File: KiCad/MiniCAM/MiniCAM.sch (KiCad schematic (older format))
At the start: 64 parts, among them J1 SMA-J-P-H-RA-TH1, J2 Conn_01x02, J3 Conn_01x03, U1 NCV8154MW180280TBG, U2 DS90UB933-Q1, U3 MT9P031, U4 SiT_2.5mmx2mm

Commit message: Finish initial schematic, layout, and routing.
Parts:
- removed C17: C_Small, .Capacitor:C_0402_1005Metric_L, symbol .Device:C_Small
- added C? (x2): 10uF, .Capacitor:C_0603_1608Metric_L, symbol .Device:C_Small
- added J4: Conn_02x03_Odd_Even, Connector_PinSocket_1.27mm:PinSocket_2x03_P1.27mm_Horizontal, symbol Connector_Generic:Conn_02x03_Odd_Even
- C11, C16: value C_Small -> 1uF
- C12: value 1uF -> 10uF; footprint .Capacitor:C_0402_1005Metric_L -> .Capacitor:C_0603_1608Metric_L
- C18, C21, C26, C29, C31: value C_Small -> 10nF
- C19, C22, C27, C30, C32: value C_Small -> 0.1uF
- C20, C23, C28: value C_Small -> 4.7uF
- C35: value ?? -> 1uF
- R7, R8: value ?? -> 10K
- R9: value ?? -> 100K
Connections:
- net labels added: DIN0, DIN1, DIN2, DIN3, DIN4, DIN5, DIN6, DIN7, DIN8, DIN9
- net labels removed: SCK
- wire segments 207 -> 221
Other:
- moved on the sheet: J3

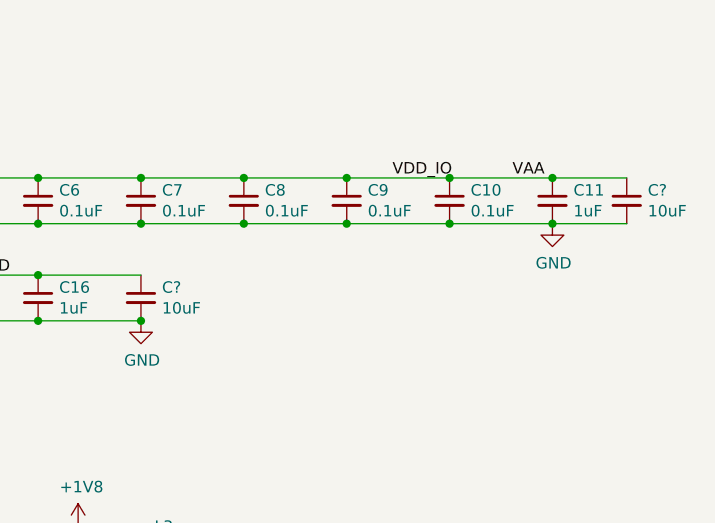
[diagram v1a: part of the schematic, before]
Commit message: Switch 2 and 3 headers from pins to sockets. Generate STEP file.
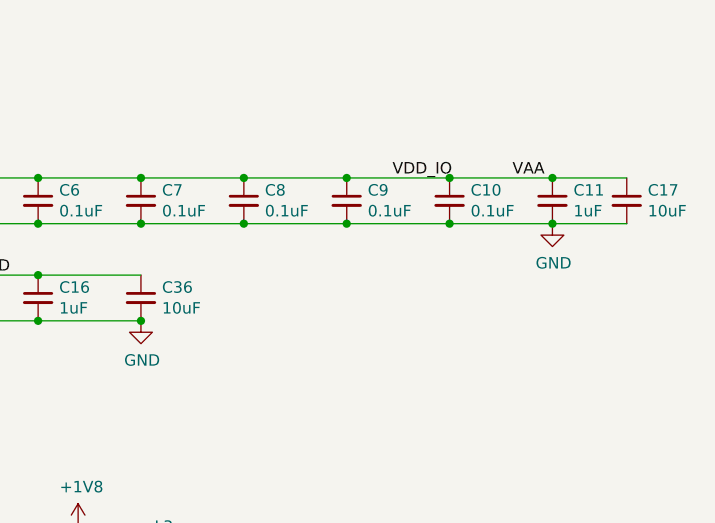
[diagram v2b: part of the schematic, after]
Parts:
- J2: footprint Connector_PinHeader_1.27mm:PinHeader_1x02_P1.27mm_Vertical -> Connector_PinSocket_1.27mm:PinSocket_1x02_P1.27mm_Vertical
- J3: footprint Connector_PinHeader_1.27mm:PinHeader_1x03_P1.27mm_Vertical -> Connector_PinSocket_1.27mm:PinSocket_1x03_P1.27mm_Vertical
- gave numbers to parts that had none: 2
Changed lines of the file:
@@
 F 0 "J2" H 5830 1417 50  0000 L CNN
 F 1 "Conn_01x02" H 5830 1326 50  0000 L CNN
-F 2 "Connector_PinHeader_1.27mm:PinHeader_1x02_P1.27mm_Vertical" H 5750 1425 50  0001 C CNN
+F 2 "Connector_PinSocket_1.27mm:PinSocket_1x02_P1.27mm_Vertical" H 5750 1425 50  0001 C CNN
 F 3 "~" H 5750 1425 50  0001 C CNN
 	1    5750 1425
@@
 F 0 "J3" H 5830 1842 50  0000 L CNN
 F 1 "Conn_01x03" H 5830 1751 50  0000 L CNN
-F 2 "Connector_PinHeader_1.27mm:PinHeader_1x03_P1.27mm_Vertical" H 5750 1800 50  0001 C CNN
+F 2 "Connector_PinSocket_1.27mm:PinSocket_1x03_P1.27mm_Vertical" H 5750 1800 50  0001 C CNN
 F 3 "~" H 5750 1800 50  0001 C CNN
 	1    5750 1800
@@
 Connection ~ 2575 1325
 $Comp
-L .Device:C_Small C?
+L .Device:C_Small C36
 U 1 1 5F776ABC
 P 8975 1350
-F 0 "C?" H 9067 1396 50  0000 L CNN
+F 0 "C36" H 9067 1396 50  0000 L CNN
 F 1 "10uF" H 9067 1305 50  0000 L CNN
 F 2 ".Capacitor:C_0603_1608Metric_L" H 8975 1350 50  0001 C CNN
@@
 Connection ~ 8975 1450
 $Comp
-L .Device:C_Small C?
+L .Device:C_Small C17
 U 1 1 5F779E53
 P 11100 925
-F 0 "C?" H 11192 971 50  0000 L CNN
+F 0 "C17" H 11192 971 50  0000 L CNN
 F 1 "10uF" H 11192 880 50  0000 L CNN
 F 2 ".Capacitor:C_0603_1608Metric_L" H 11100 925 50  0001 C CNN

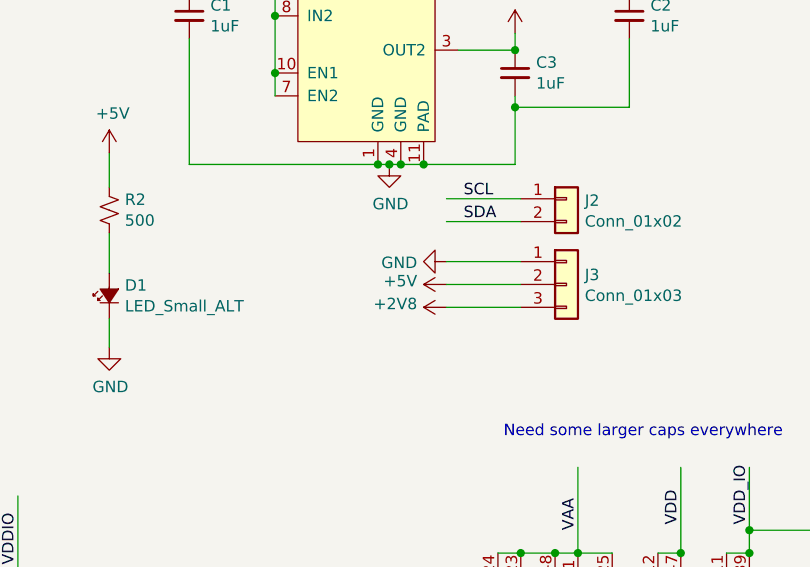
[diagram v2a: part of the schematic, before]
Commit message: Move LED ring headers to a consistent 4mm x 1mm spacing from center on lens.
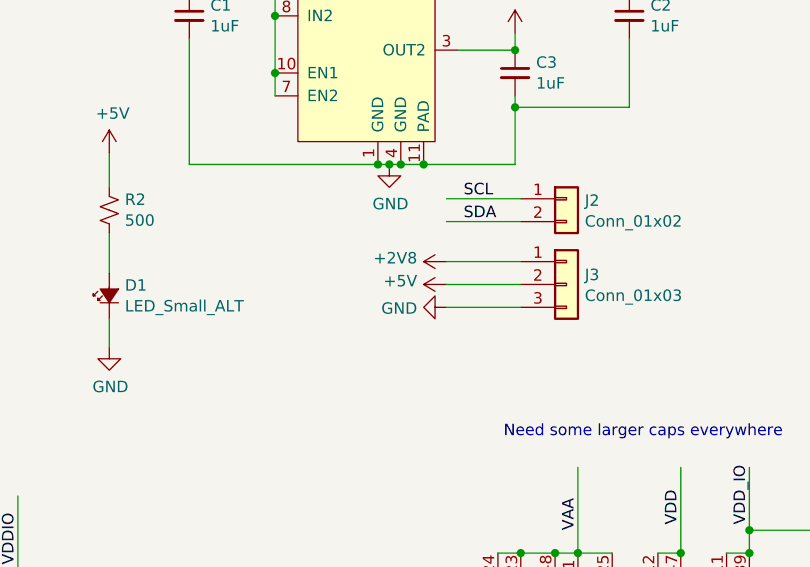
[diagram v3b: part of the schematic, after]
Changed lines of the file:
@@
 L power:GND #PWR0138
 U 1 1 5F6758D2
-P 5225 1700
-F 0 "#PWR0138" H 5225 1450 50  0001 C CNN
-F 1 "GND" V 5230 1572 50  0000 R CNN
-F 2 "" H 5225 1700 50  0001 C CNN
-F 3 "" H 5225 1700 50  0001 C CNN
-	1    5225 1700
+P 5225 1900
+F 0 "#PWR0138" H 5225 1650 50  0001 C CNN
+F 1 "GND" V 5230 1772 50  0000 R CNN
+F 2 "" H 5225 1900 50  0001 C CNN
+F 3 "" H 5225 1900 50  0001 C CNN
+	1    5225 1900
 	0    1    1    0
 $EndComp
@@
 L power:+2V8 #PWR0140
 U 1 1 5F67654A
-P 5225 1900
-F 0 "#PWR0140" H 5225 1750 50  0001 C CNN
-F 1 "+2V8" V 5240 2028 50  0000 L CNN
-F 2 "" H 5225 1900 50  0001 C CNN
-F 3 "" H 5225 1900 50  0001 C CNN
-	1    5225 1900
+P 5225 1700
+F 0 "#PWR0140" H 5225 1550 50  0001 C CNN
+F 1 "+2V8" V 5240 1828 50  0000 L CNN
+F 2 "" H 5225 1700 50  0001 C CNN
+F 3 "" H 5225 1700 50  0001 C CNN
+	1    5225 1700
 	0    -1   -1   0
 $EndComp

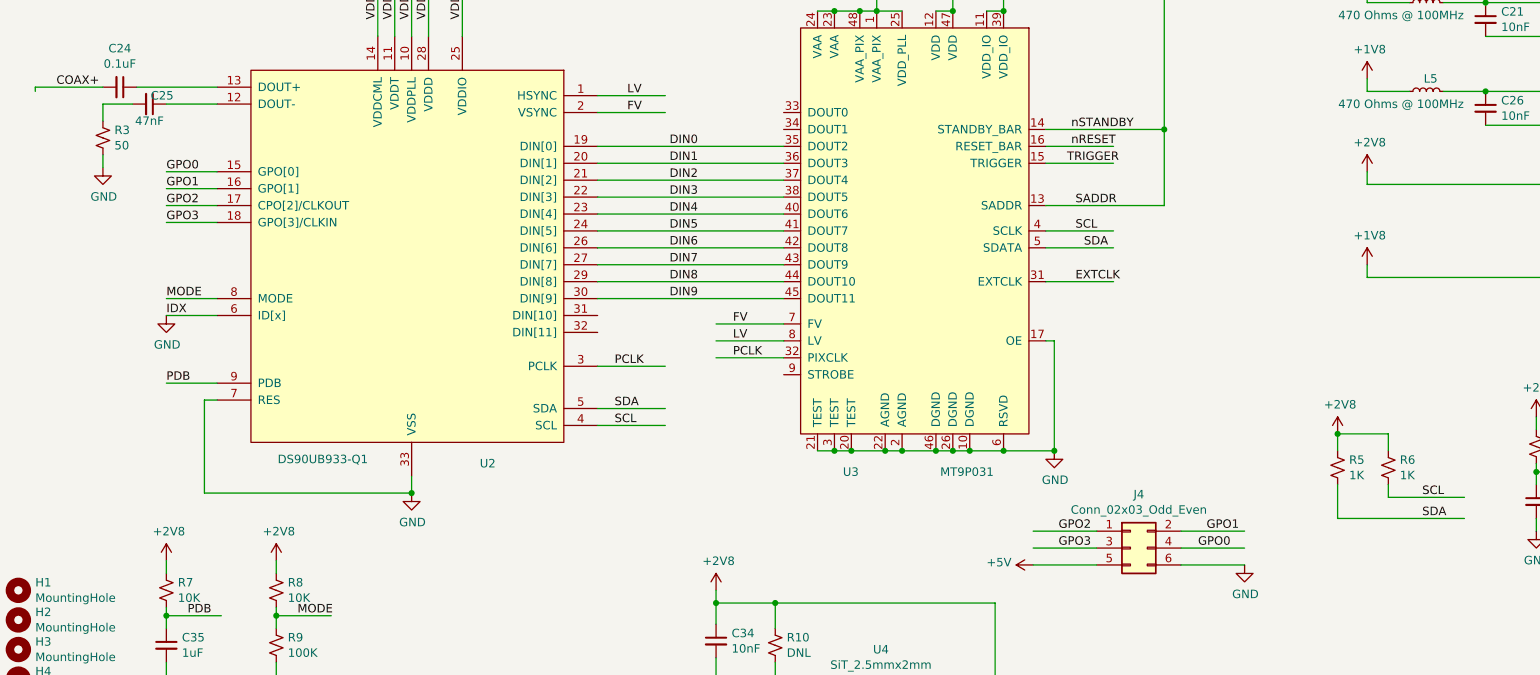
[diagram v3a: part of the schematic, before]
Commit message: Updated LED ring PCB Board
Changed 10UF 0603 to 1210 50V: C1210C106K5RACTU
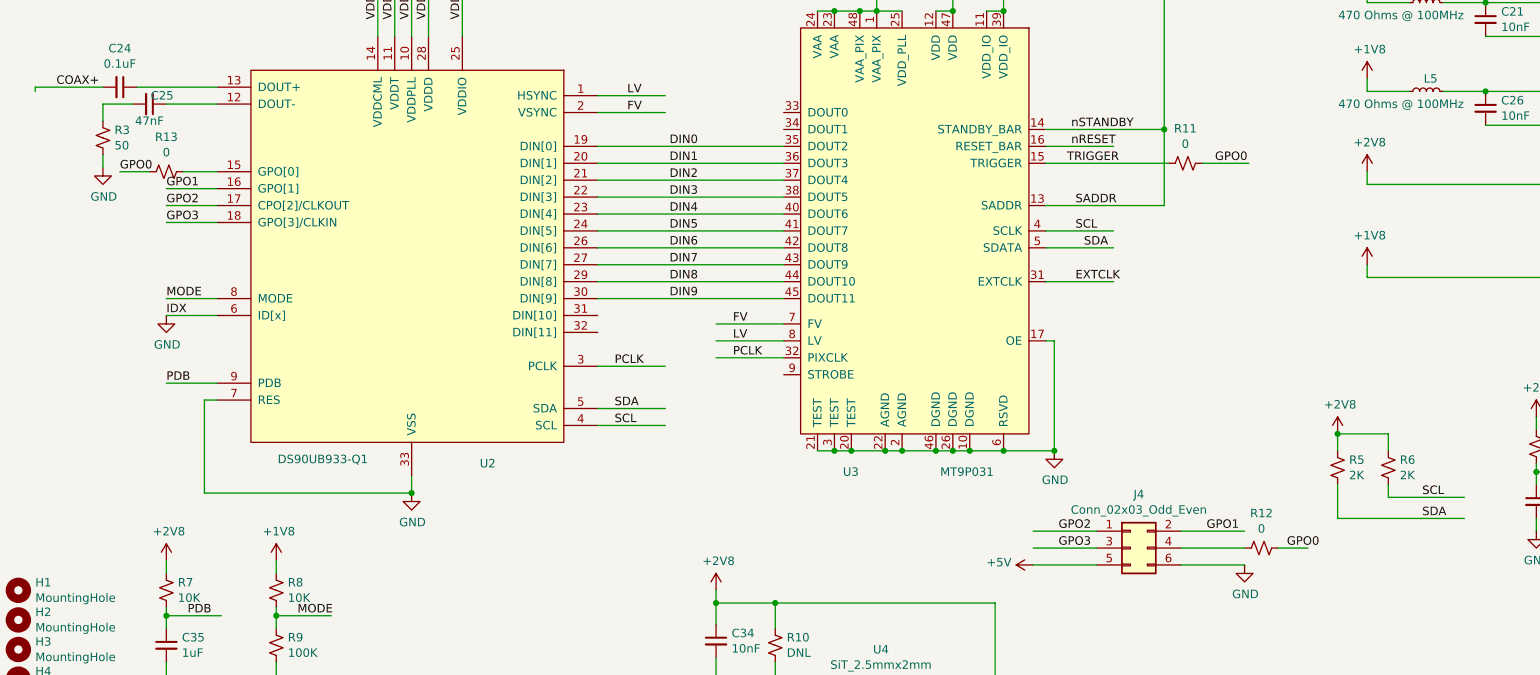
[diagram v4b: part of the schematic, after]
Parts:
- added R11, R12, R13: 0, .Resistor:R_0402_1005Metric_ERJ_L, symbol .Device:R_Small_US
- C1, C11, C16, C2, C3, C33, C35: Part Number (none) -> GRT155R61C105KE01D
- C10, C14, C15, C19, C22, C24, C27, C30, C32, C4, C5, C6, C7, C8, C9: Part Number (none) -> GCM155R71C104KA55J
- C12, C13, C17, C36: Part Number (none) -> GRM188R61A106KE69J
- C18, C21, C26, C29, C31, C34: Part Number (none) -> GCM155R71E103KA37D
- C20, C23, C28: Part Number (none) -> CC0402MRX5R6BB475
- C25: Part Number (none) -> GRM155R71A473KA01D
- D1: Part Number (none) -> LTST-C190KRKT
- H1, H2, H3, H4, H5, H6, J2, J3, J4, R10, U3, U4: Part Number (none) -> DNL
- J1: Part Number (none) -> CONSMA001-SMD-G-T
- L1, L3, L4, L5: Part Number (none) -> BLM18PG471SN1D
- L2: Part Number (none) -> ADL3225V-470MT-TL000
- R1: Part Number (none) -> ERJ-2RKF2001X
- R2: Part Number (none) -> ERJ-2RKF4990X
- R3: Part Number (none) -> ERJ-2RKF49R9X
- R4: Part Number (none) -> ERJ-2GEJ102X
- R5, R6: value 1K -> 2K; Part Number (none) -> ERJ-2RKF2001X
- R7, R8: Part Number (none) -> ERJ-2RKF1002X
- R9: Part Number (none) -> ERJ-2RKF1003X
- U1: Part Number (none) -> NCV8154MW180280TBG
- U2: Part Number (none) -> DS90UB913ATRTVTQ1
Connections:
- wire segments 221 -> 224

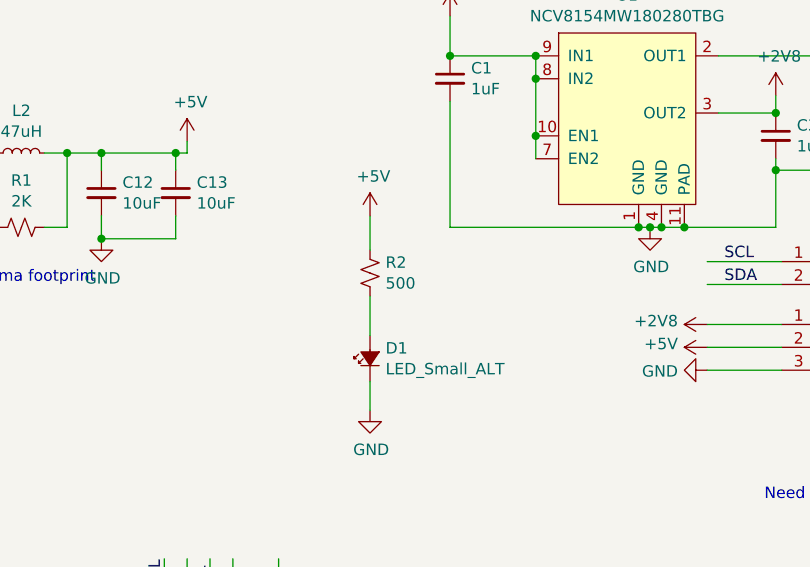
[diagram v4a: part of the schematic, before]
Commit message: Correct minor error on top silk screen. Change to rev v1.0
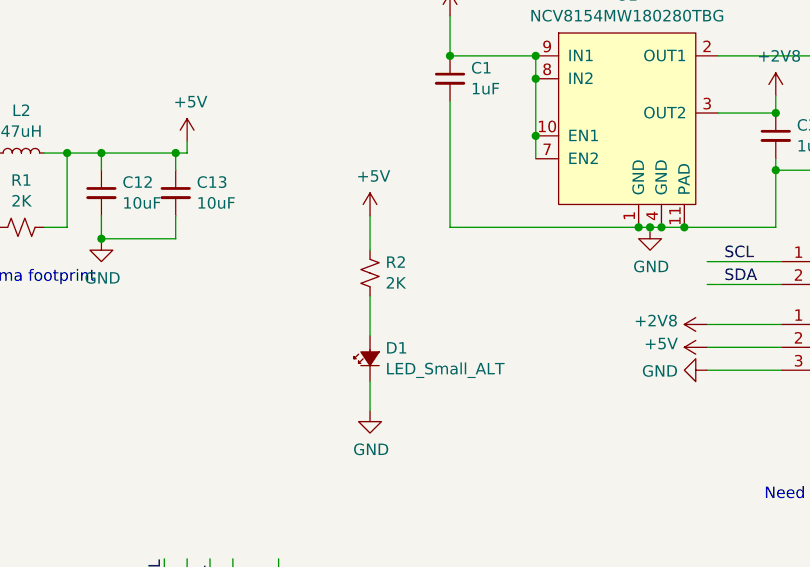
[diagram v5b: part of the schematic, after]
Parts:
- R2: value 500 -> 2K; Part Number ERJ-2RKF4990X -> ERJ-2RKF2001X
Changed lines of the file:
@@
 Sheet 1 1
 Title ""
-Date "2020-07-21"
-Rev "v0.1"
+Date "2020-09-01"
+Rev "v1.0"
 Comp "Aharoni Lab"
 Comment1 ""
@@
 	1    3750 1850
 	0    -1   -1   0
-$EndComp
-$Comp
-L .Device:R_Small_US R2
-U 1 1 5F138425
-P 3750 1475
-F 0 "R2" H 3818 1521 50  0000 L CNN
-F 1 "500" H 3818 1430 50  0000 L CNN
-F 2 ".Resistor:R_0402_1005Metric_ERJ_L" H 3750 1475 50  0001 C CNN
-F 3 "~" H 3750 1475 50  0001 C CNN
-F 4 "ERJ-2RKF4990X" H 3750 1475 50  0001 C CNN "Part Number"
-	1    3750 1475
-	1    0    0    -1
 $EndComp
 $Comp
@@
 	1    0    0    -1
 $EndComp
+$Comp
+L .Device:R_Small_US R2
+U 1 1 5F138425
+P 3750 1475
+F 0 "R2" H 3818 1521 50  0000 L CNN
+F 1 "2K" H 3818 1430 50  0000 L CNN
+F 2 ".Resistor:R_0402_1005Metric_ERJ_L" H 3750 1475 50  0001 C CNN
+F 3 "~" H 3750 1475 50  0001 C CNN
+F 4 "ERJ-2RKF2001X" H 3750 1475 50  0001 C CNN "Part Number"
+	1    3750 1475
+	1    0    0    -1
+$EndComp

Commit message: Update output files and check part numbers for v1.0 fabrication
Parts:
- U3: Part Number DNL -> MT9P031I12STM
- U4: Part Number DNL -> DSC1001DI2-096.0000
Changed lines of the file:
@@
 F 2 ".Package_LCC:iLCC48P70_1000X1000X135L80X40N" H 6150 4875 50  0001 C CNN
 F 3 "https://www.onsemi.com/pub/Collateral/MT9P031-D.PDF" H 6150 4875 50  0001 C CNN
-F 4 "DNL" H 6050 4275 50  0001 C CNN "Part Number"
+F 4 "MT9P031I12STM" H 6050 4275 50  0001 C CNN "Part Number"
 	1    6050 4275
 	-1   0    0    -1
@@
 F 2 ".Oscillator:OSC_CC250X200X80L70X75L" H 5775 7325 50  0001 C CNN
 F 3 "https://www.sitime.com/datasheet/SiT8008" H 5775 7325 50  0001 C CNN
-F 4 "DNL" H 5825 7075 50  0001 C CNN "Part Number"
+F 4 "DSC1001DI2-096.0000" H 5825 7075 50  0001 C CNN "Part Number"
 	1    5825 7075
 	1    0    0    -1
